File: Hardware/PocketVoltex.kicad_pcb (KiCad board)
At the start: 2 copper layers, 168 x 109.2 mm, 74 parts, among them J1 Programming header, J2 USB_C_Receptacle, SW1 MX socket, SW2 MX socket, SW3 MX socket, SW4 MX socket, SW5 MX socket, SW6 MX socket, SW7 MX socket, SW8 SW_Push, U1 ATMEGA16U2-AU, X1 16MHz

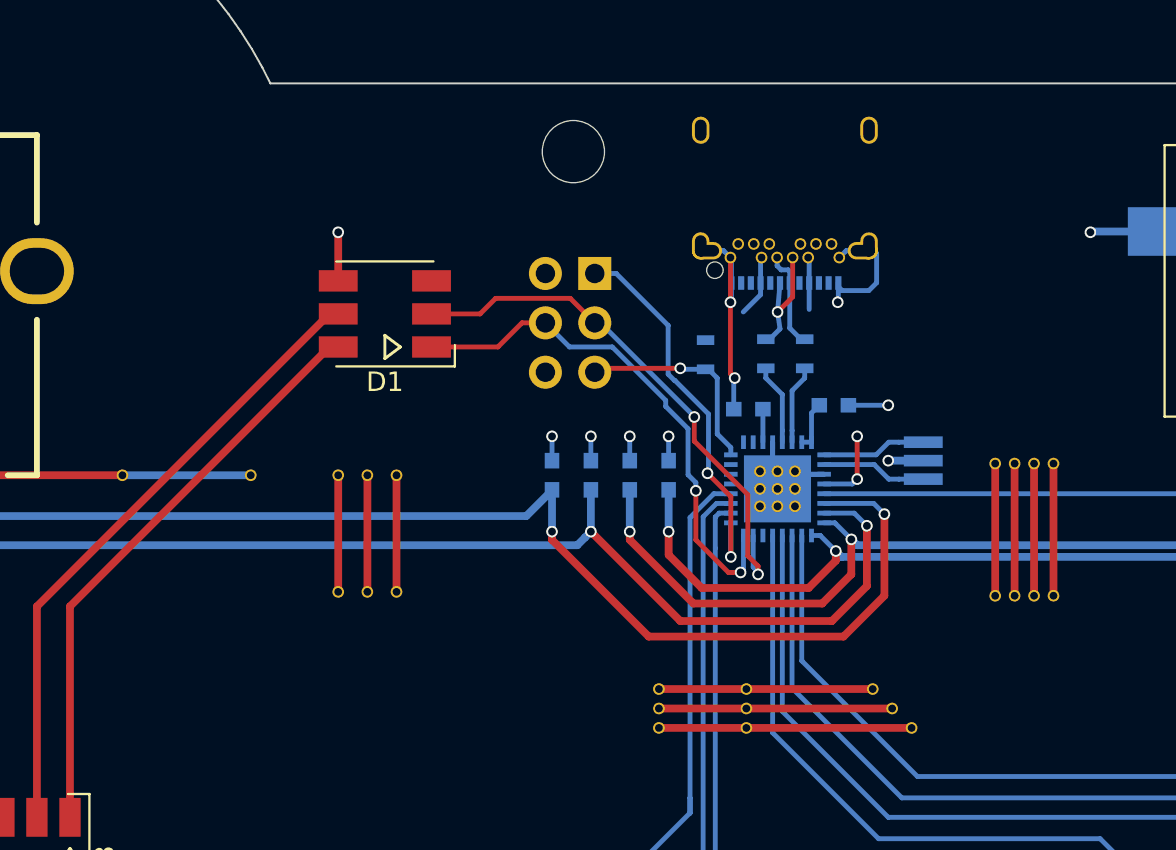
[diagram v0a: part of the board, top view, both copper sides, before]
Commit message: Kicad 5.1, USB 2.0 C receptacle, CC pulldown
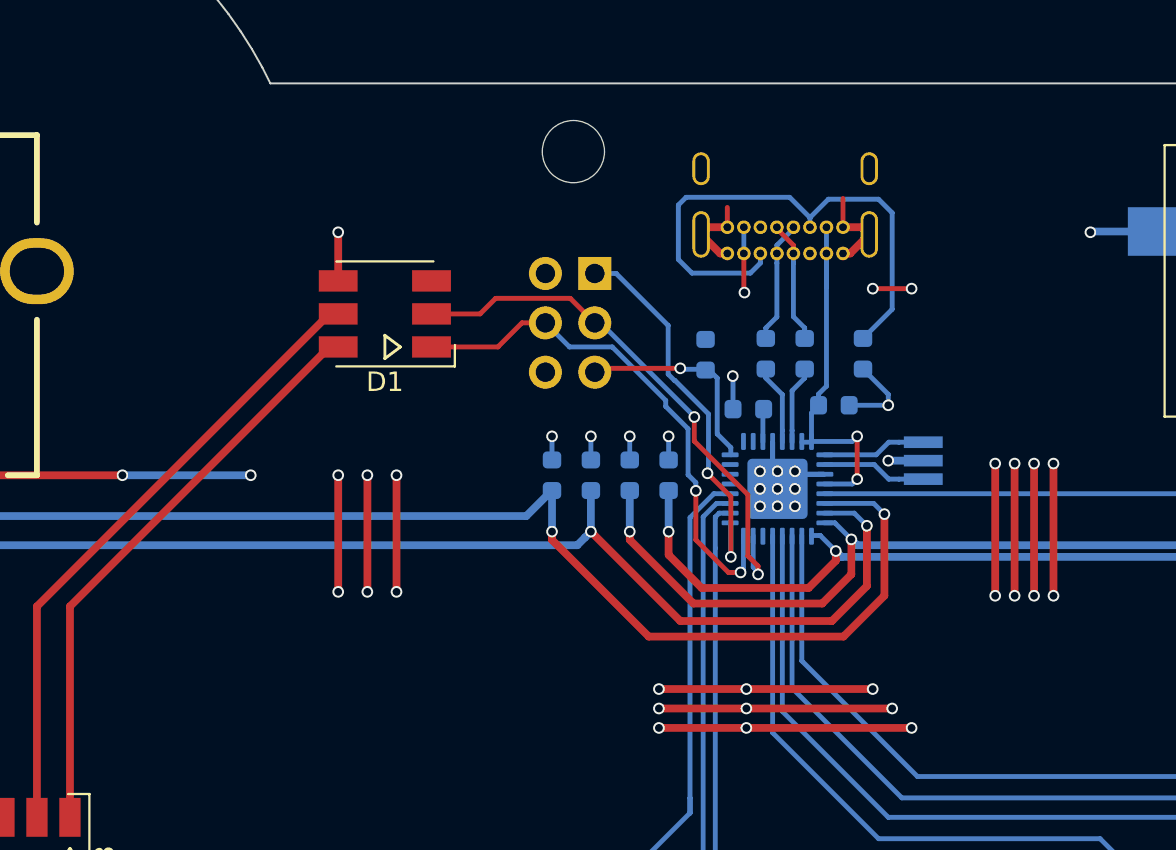
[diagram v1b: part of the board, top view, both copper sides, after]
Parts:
- removed REF** (x34): VIA_0.4mm, Pocket Voltex:VIA_0.4mm
- added R4: 5.1k, Resistor_SMD:R_0603_1608Metric, B.Cu at (132.7, 69.8)
- C1, C2, C3, C4, C5, C6: footprint Capacitors_SMD:C_0603 -> Capacitor_SMD:C_0603_1608Metric
- H1, H2, H3, H4, H5, H6, H7, H8: renamed from ?; value MountingHole_3.2mm_M3 -> MountingHole; footprint Mounting_Holes:MountingHole_3.2mm_M3 -> MountingHole:MountingHole_3.2mm_M3
- J1: footprint Pin_Headers:Pin_Header_Straight_2x03_Pitch2.54mm -> Connector_PinHeader_2.54mm:PinHeader_2x03_P2.54mm_Vertical
- J2: footprint Pocket Voltex:USB_C_Receptacle_UJ31-CH-31-SMT-TR -> Pocket Voltex:USB_C_Receptacle_GCT_USB4085
- LOGO1: renamed from G***; value LOGO -> Rasis
- R1, R2, R3: footprint Resistors_SMD:R_0603 -> Resistor_SMD:R_0603_1608Metric
- U1: value ATMEGA16U2-AU -> ATmega16U2-MU; footprint Housings_DFN_QFN:QFN-32-1EP_5x5mm_Pitch0.5mm -> Package_DFN_QFN:QFN-32-1EP_5x5mm_P0.5mm_EP3.1x3.1mm
- moved J2 3.33 mm to (125.7, 64.6)
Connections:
- J2 pad B5: Net-(J2-PadB5) -> Net-(J2-PadA5)
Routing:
- net Net-(J2-PadA5): track 0.00 -> 27.9 mm
- net VCC: track 117.4 -> 130.4 mm, vias 10 -> 36
- net GND: track 92.7 -> 86.5 mm, vias 18 -> 27
- net /D-: track 5.12 -> 6.31 mm
- net /D+: track 6.44 -> 6.31 mm, vias 1 -> 0

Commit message: Change rev to 8
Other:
- board text added: "2019 Rev 8"
- board text removed: "2018 Rev 7"
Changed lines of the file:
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@@
     (effects (font (size 1.5 1.5) (thickness 0.3)) (justify mirror))
   )
-  (gr_text "2018\nRev 7" (at 155.2 96.2) (layer B.SilkS)
+  (gr_text "2019\nRev 8" (at 155.2 96.2) (layer B.SilkS)
     (effects (font (size 1.5 1.5) (thickness 0.3)) (justify mirror))
   )

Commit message: Commit all the in-progress stuff for a clean slate
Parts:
- added EH1: Encoder nut, Pocket Voltex:SMD_Standoff_M2_Wurth, B.Cu at (82.2, 76.8)
- added EH2: Encoder nut, Pocket Voltex:SMD_Standoff_M2_Wurth, B.Cu at (82.2, 54.2)
- added EH3: Encoder nut, Pocket Voltex:SMD_Standoff_M2_Wurth, B.Cu at (228.2, 76.8)
- added EH4: Encoder nut, Pocket Voltex:SMD_Standoff_M2_Wurth, B.Cu at (228.2, 54.2)
- added EJ1: Hotswap, Pocket Voltex:Harwin-SMD-Socket-S9091-46R, F.Cu at (92.7, 70.5)
- added EJ2: Hotswap, Pocket Voltex:Harwin-SMD-Socket-S9091-46R, F.Cu at (92.7, 65.5)
- added EJ3: Hotswap, Pocket Voltex:Harwin-SMD-Socket-S9091-46R, F.Cu at (92.7, 60.5)
- added EJ4: Hotswap, Pocket Voltex:Harwin-SMD-Socket-S9091-46R, F.Cu at (217.7, 60.5)
- added EJ5: Hotswap, Pocket Voltex:Harwin-SMD-Socket-S9091-46R, F.Cu at (217.7, 65.5)
- added EJ6: Hotswap, Pocket Voltex:Harwin-SMD-Socket-S9091-46R, F.Cu at (217.7, 70.5)
- ENC1, ENC2: footprint Pocket Voltex:Encoder_Bourns_PEC16 -> Pocket Voltex:Encoder_Bourns_PEC16_hotswap
- U1: value ATmega16U2-MU -> ATmega32U2-AU; footprint Package_DFN_QFN:QFN-32-1EP_5x5mm_P0.5mm_EP3.1x3.1mm -> Package_QFP:TQFP-32_7x7mm_P0.8mm
- moved C5 16.2 mm to (138.1, 81.0)
- moved C6 16.2 mm to (136.1, 81.0)
- moved U1 2.86 mm to (128.0, 79.5)
- moved X1 2.52 mm to (137.4, 77.2)
- turned C1 to 180 degrees
- turned ENC1 to 90 degrees
- turned ENC2 to 270 degrees
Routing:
- net VCC: track 130.4 -> 179.3 mm, vias 36 -> 48
- net /ENC2B: track 119.0 -> 96.6 mm, vias 2 -> 1
- net /ENC1A: track 67.9 -> 53.9 mm, vias 2 -> 3
- net /ENC1B: track 66.1 -> 58.3 mm, vias 2 -> 3
- net /ENC2A: track 109.1 -> 114.8 mm, vias 2 -> 3
- net (no net): track 0.00 -> 5.08 mm
- net /SW_D: track 86.6 -> 81.8 mm
- net /SW_C: track 59.4 -> 54.6 mm
- net GND: track 86.5 -> 90.7 mm, vias 27 -> 22
- net /SW_A: track 25.9 -> 21.8 mm
- net /SW_B: track 34.0 -> 30.7 mm
- net /SW_FXR: track 95.4 -> 92.5 mm
- net /SCLK: track 27.9 -> 30.7 mm, vias 2 -> 1
- net /MOSI: track 27.0 -> 29.7 mm, vias 2 -> 1
- net /MISO: track 19.9 -> 21.8 mm
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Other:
- board text added: "2020 Rev 8"
- board text added: "Replace with Bourns PEC16-4020F-N0024"
- board text removed: "2019 Rev 8"
